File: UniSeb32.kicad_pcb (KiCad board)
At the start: 4 copper layers, 72 x 100 mm, 53 parts, among them J1 IO, J101 Micro_SD_Card_Det, J2 ARJM11C7-114-BA-EW2, J3 Conn_02x05_Odd_Even, J6 SDS011, J7 Conn_01x02_Female, J8 Conn_01x02_Female, U1 mini_esp32, U101 RTL8201F-VB-CG, U3 AMS1117-3.3, U4 AMS5915, U5 module_bme280, U6 RT9400, U7 MCP23008-xSS, U8 HLK-PM01, X1 233-508, X2 233-503, X3 233-504

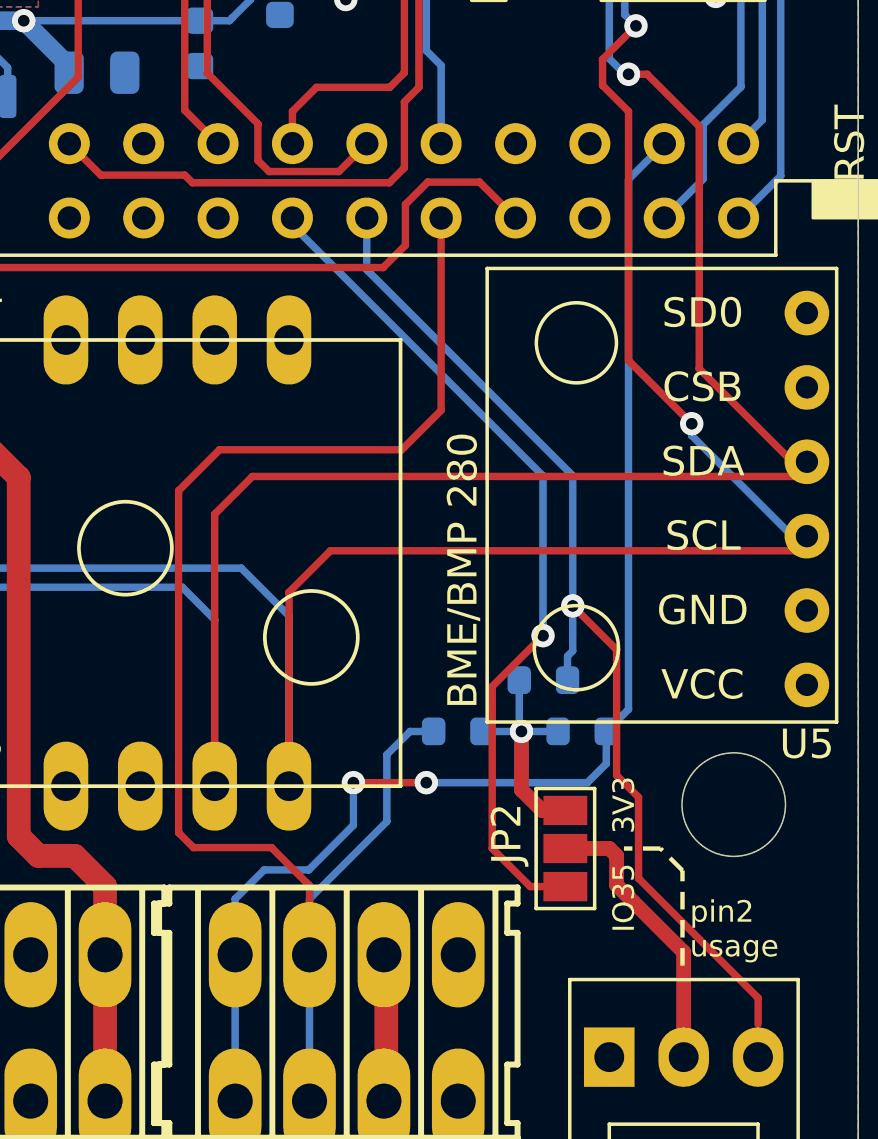
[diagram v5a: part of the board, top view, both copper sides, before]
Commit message: Changed JP2-fixed voltage option (3.3V) to flexible voltage (3.3V/5V) with JP3
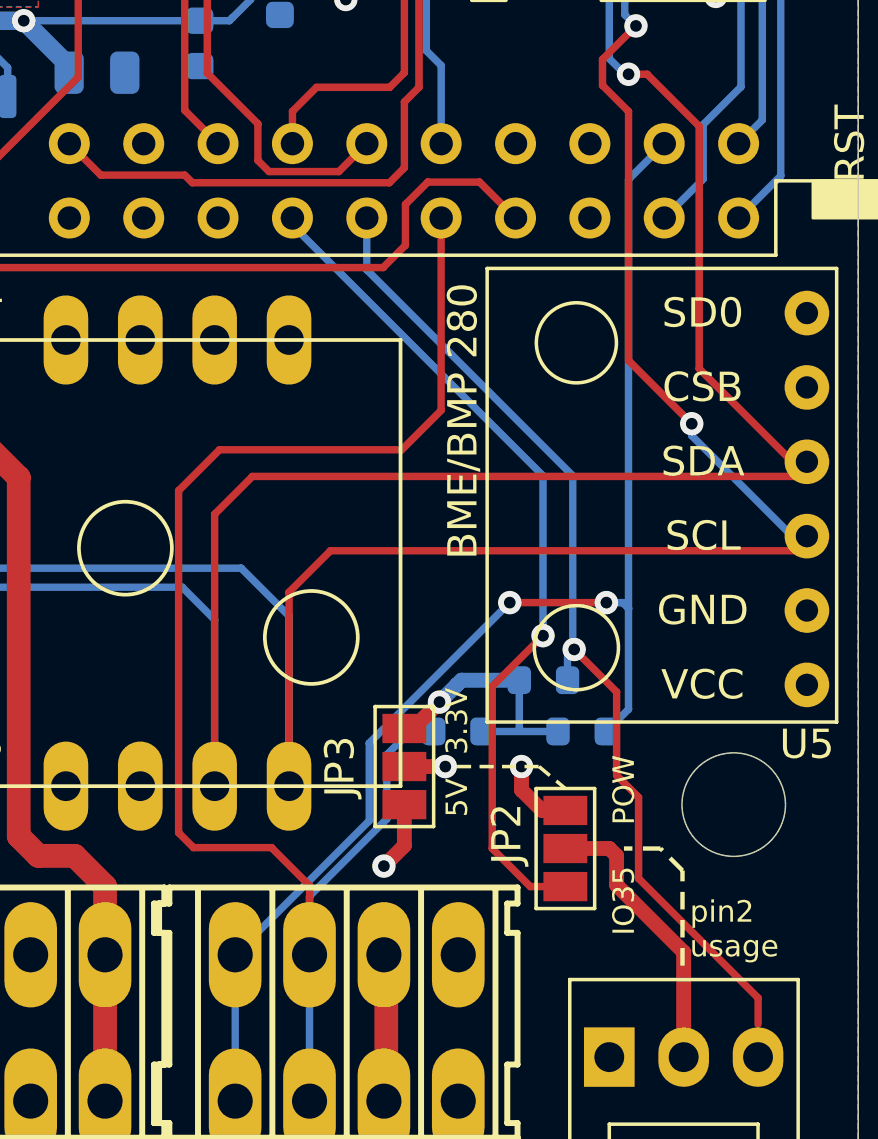
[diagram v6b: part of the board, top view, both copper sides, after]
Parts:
- added JP3: SolderJumper_3_Open, Jumper:SolderJumper-3_P1.3mm_Open_Pad1.0x1.5mm_NumberLabels, F.Cu at (169.0, 130.2)
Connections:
- JP2 pad 1: +3.3V -> Net-(JP2-A)
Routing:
- net Net-(JP2-A): track 0.00 -> 6.59 mm, vias 0 -> 2
- net +5V: track 226.2 -> 231.7 mm, vias 2 -> 3
- net /IO33: track 35.9 -> 34.2 mm
- net /ONEWIRE: track 44.3 -> 45.9 mm
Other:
- board text added: "3.3V"
- board text added: "5V"
- board text added: "POW"
- board text removed: "3V3"
